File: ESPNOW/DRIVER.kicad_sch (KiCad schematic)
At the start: 7 parts, among them U2 DRV8848

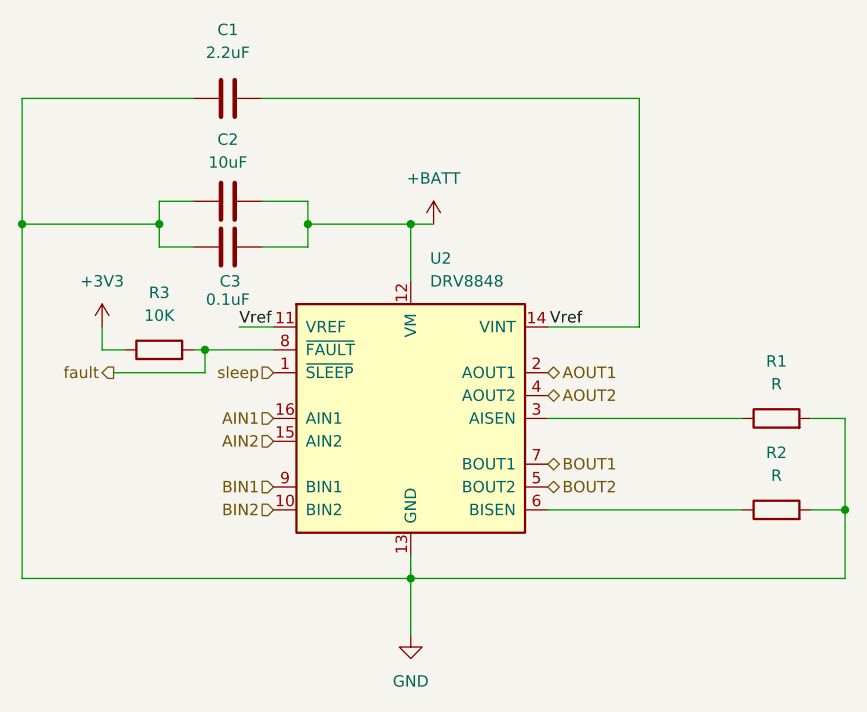
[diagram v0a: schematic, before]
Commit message: Third Iteration
Reworked general layout to reduce size

Reworked Motor Driver routing to comply with layout guidelines in datasheet

Reworked Buck Converter routing to comply with layout guidelines in datasheet

TODO:
Add info to back layer
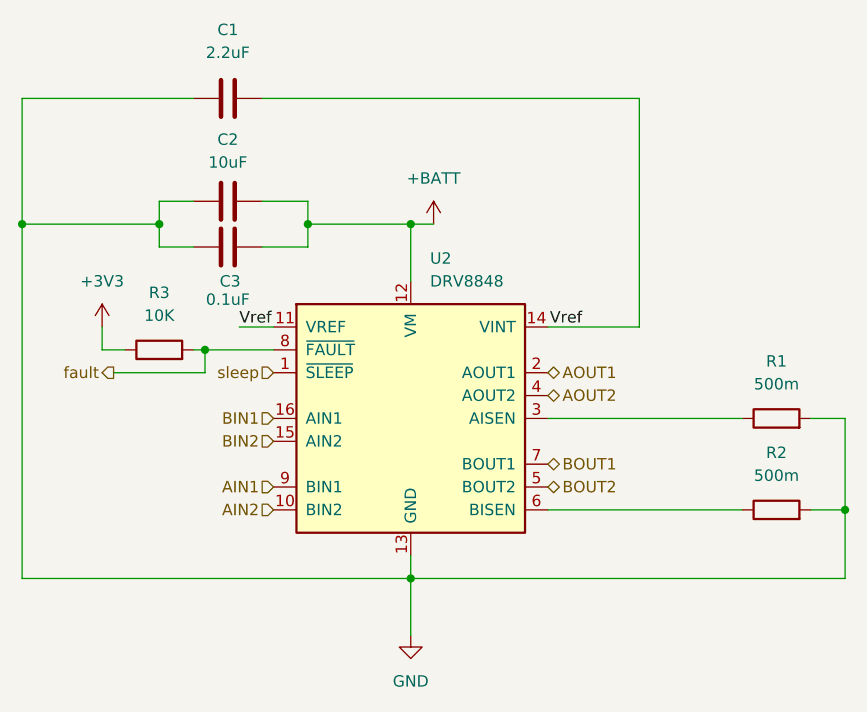
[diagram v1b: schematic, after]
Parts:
- R1, R2: value R -> 500m
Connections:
- net AIN1: now also U2.9 (BIN1); no longer U2.16 (AIN1)
- net AIN2: now also U2.10 (BIN2); no longer U2.15 (AIN2)
- net BIN1: now also U2.16 (AIN1); no longer U2.9 (BIN1)
- net BIN2: now also U2.15 (AIN2); no longer U2.10 (BIN2)
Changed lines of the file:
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@@
+		)
+	)
+	(hierarchical_label "BIN1"
+		(shape input)
+		(at 129.54 96.52 180)
+		(effects
+			(font
+				(size 1.27 1.27)
+			)
+			(justify right)
+		)
+	)
+	(hierarchical_label "BIN2"
+		(shape input)
+		(at 129.54 99.06 180)
+		(effects
+			(font
+				(size 1.27 1.27)
+			)
+			(justify right)
 		)
 	)
@@
 		)
 	)
-	(hierarchical_label "BIN2"
+	(hierarchical_label "AIN2"
 		(shape input)
 		(at 129.54 106.68 180)
@@
 	(hierarchical_label "AIN1"
 		(shape input)
-		(at 129.54 96.52 180)
+		(at 129.54 104.14 180)
 		(effects
 			(font
@@
 		)
 	)
-	(hierarchical_label "AIN2"
-		(shape input)
-		(at 129.54 99.06 180)
-		(effects
-			(font
-				(size 1.27 1.27)
-			)
-			(justify right)
-		)
-	)
-	(hierarchical_label "BIN1"
-		(shape input)
-		(at 129.54 104.14 180)
-		(effects
-			(font
-				(size 1.27 1.27)
-			)
-			(justify right)
-		)
-	)
 	(symbol
 		(lib_id "Driver_Motor:DRV8848")
@@
 			)
 		)
-		(property "Value" "R"
+		(property "Value" "500m"
 			(at 185.42 92.71 90)
 			(effects
@@
 			)
 		)
-		(property "Value" "R"
+		(property "Value" "500m"
 			(at 185.42 102.87 90)
 			(effects
